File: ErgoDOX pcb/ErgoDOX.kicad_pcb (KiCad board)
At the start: 2 copper layers, 182.8 x 158.9 mm, 74 parts, among them J1 USB, J2 3.5mm, J3 JMP, J4 JMP, SW0:10 SW0:3, SW0:11 SW0:2, SW0:12 SW0:1, SW0:7 SW0:6, SW0:8 SW0:5, SW0:9 SW0:4, SW1:10 SW1:3, SW1:11 SW1:2, SW1:12 SW1:1, SW1:13 SW1:0, SW1:9 SW1:4, SW2:10 SW2:3, SW2:11 SW2:2, SW2:12 SW2:1, SW2:13 SW2:0, SW2:7 SW2:6, SW2:8 SW2:5, SW2:9 SW2:4, SW3:10 SW3:3, SW3:11 SW3:2, SW3:12 SW3:1, SW3:13 SW3:0, SW3:8 SW3:5, SW3:9 SW3:4, SW4:10 SW4:3, SW4:11 SW4:2, SW4:12 SW4:1, SW4:13 SW4:0, SW4:7 SW4:6, SW4:8 SW4:5, SW4:9 SW4:4, SW5:10 SW5:3, SW5:11 SW5:2, SW5:12 SW5:1, SW5:13 SW5:0, SW5:7 SW5:6, SW5:8 SW5:5, SW5:9 SW5:4, U1 TEENSY2.0, U2 MCP23018

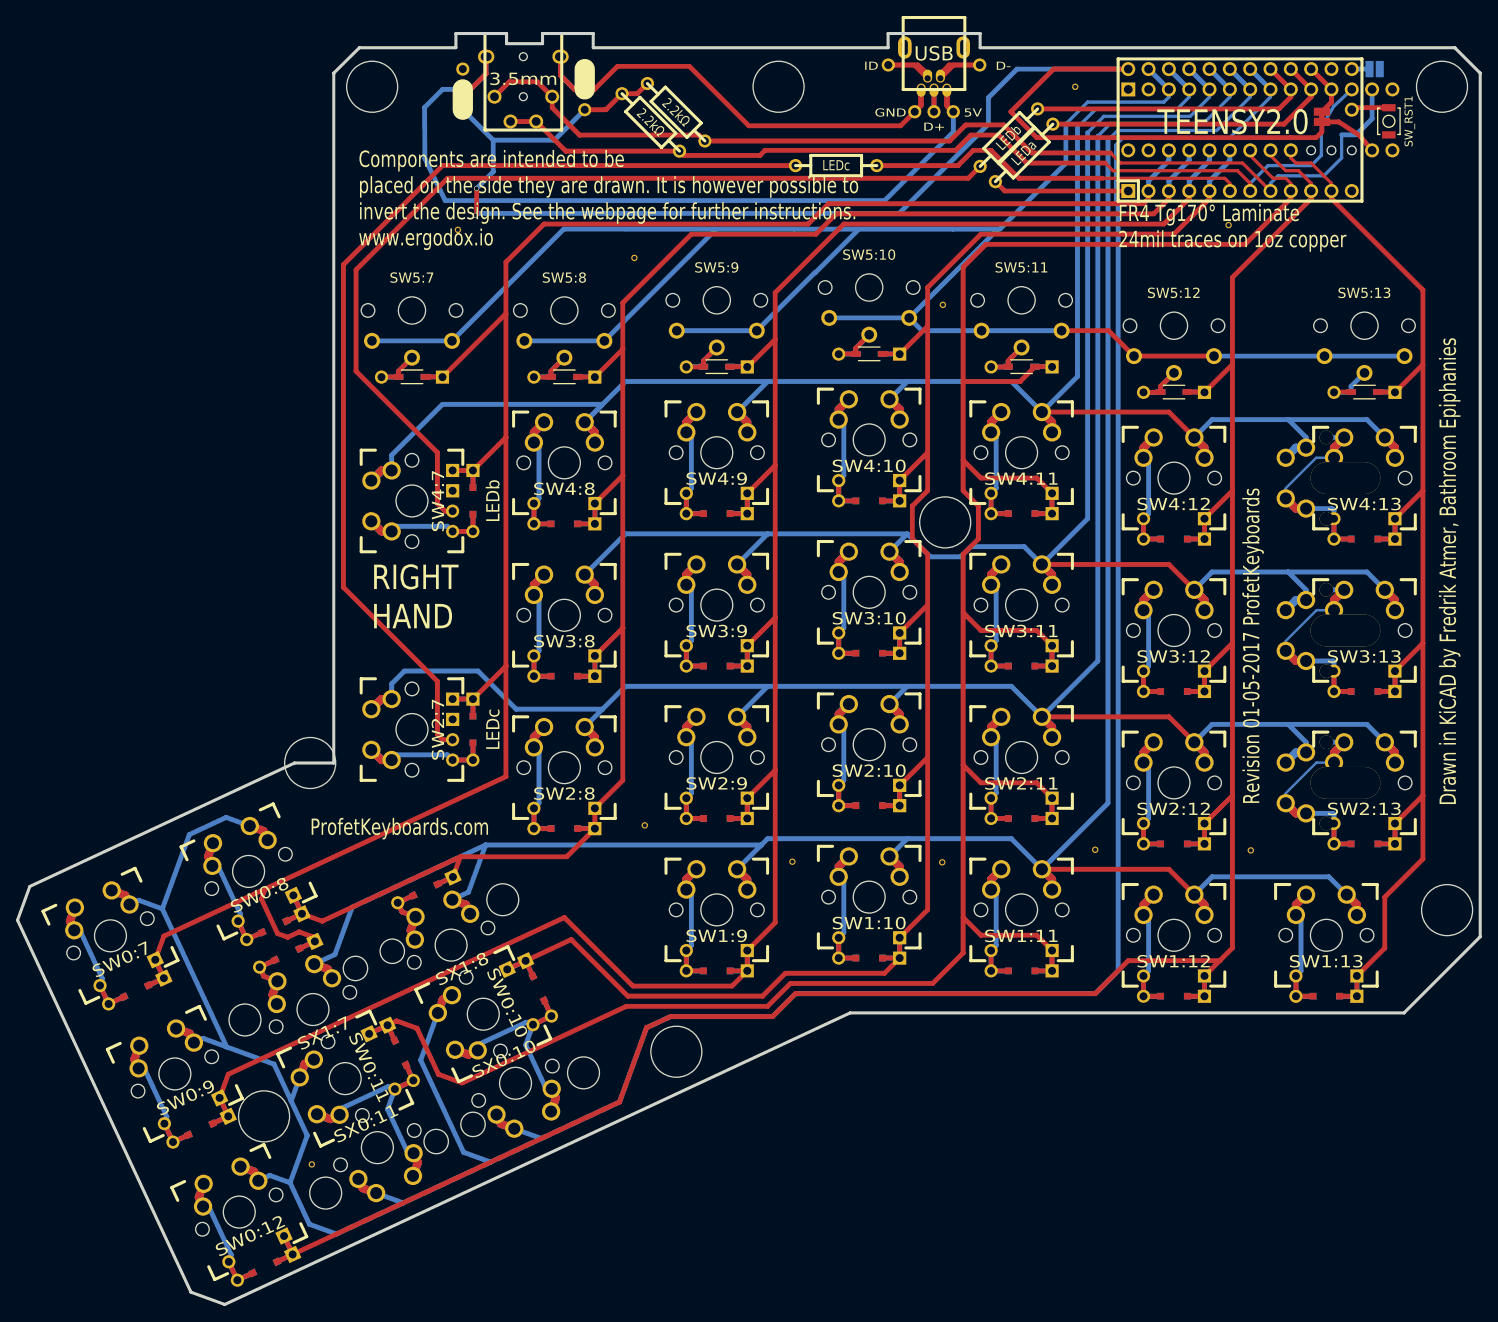
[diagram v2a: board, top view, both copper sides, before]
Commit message: finish replacing all switches
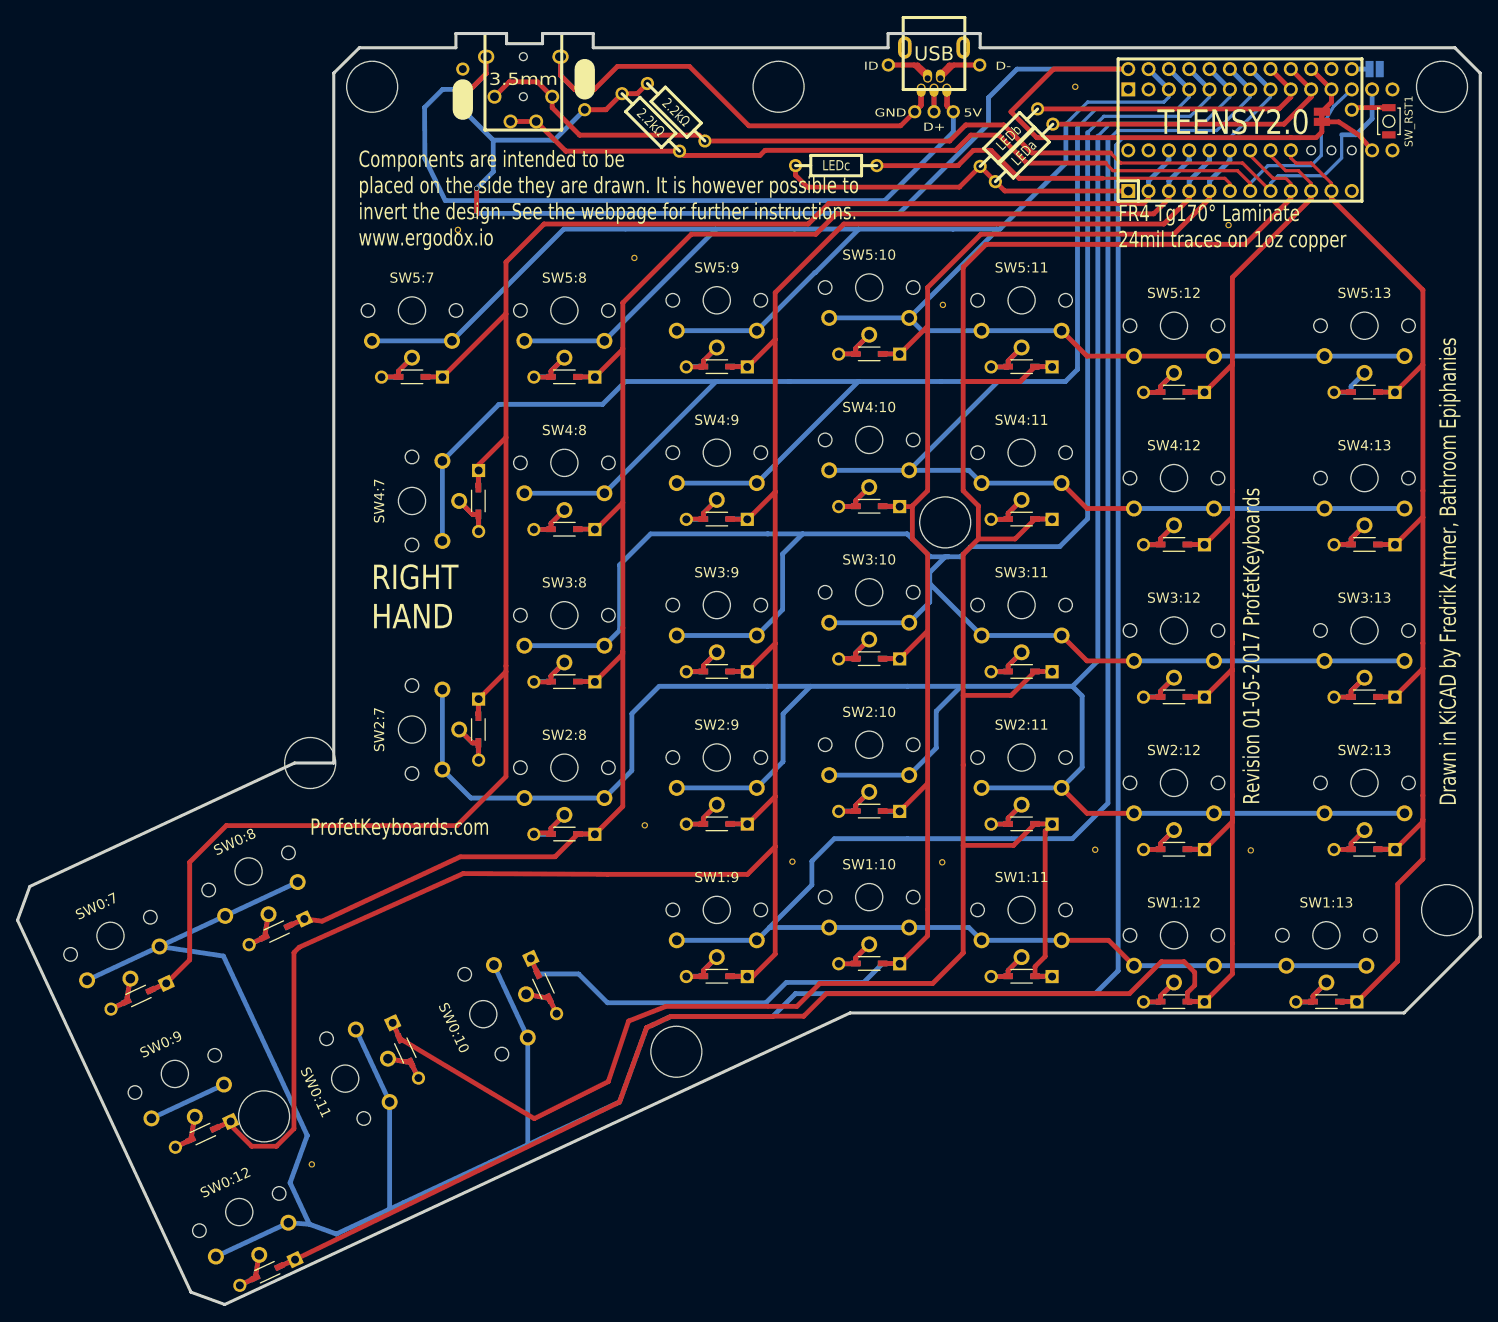
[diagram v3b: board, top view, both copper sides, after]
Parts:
- removed D1:7, D1:8: D, DIODE
- removed LED_B1: LEDb, MX_LED
- removed LED_C1: LEDc, MX_LED
- removed S1, S2: STAB200, STAB_PCB940
- removed SX0:10: SX0:3, MX_FLIP
- removed SX0:11: SX0:2, MX_FLIP
- removed SX1:7: SX1:6, MX_FLIP
- removed SX1:8: SX1:5, MX_FLIP
- SW0:10, SW0:11, SW0:12, SW0:7, SW0:8, SW0:9, SW1:10, SW1:11, SW1:12, SW1:13, SW1:9, SW2:10, SW2:11, SW2:12, SW2:7, SW2:8, SW2:9, SW3:10, SW3:11, SW3:12, SW3:8, SW3:9, SW4:10, SW4:11, SW4:12, SW4:7, SW4:8, SW4:9: footprint ErgoDOX pcb:MX_FLIP_DIODE -> ErgoDOX pcb:SW_choc_Reversible_1u
- SW2:13, SW3:13, SW4:13: footprint ErgoDOX pcb:MX_FLIP_XX -> ErgoDOX pcb:SW_choc_Reversible_1u
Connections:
- RB1 pad 2: Net-(LED_B1-Pad1) -> GND
- RC1 pad 2: Net-(LED_C1-Pad1) -> GND
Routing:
- net Net-(LED_C1-Pad1): track 127.4 -> 0.00 mm
- net Net-(LED_B1-Pad1): track 119.1 -> 0.00 mm
- net /ROW1: track 318.2 -> 246.8 mm
- net /ROW4: track 257.4 -> 292.0 mm
- net GND: track 19.3 -> 48.0 mm
- net Net-(SW3:13-Pad2): track 35.2 -> 10.4 mm
- net Net-(SW2:13-Pad2): track 35.2 -> 10.4 mm
- net Net-(SW4:13-Pad2): track 35.2 -> 10.4 mm
- net Net-(SW0:11-Pad2): track 34.8 -> 10.1 mm
- net Net-(SW0:10-Pad2): track 34.8 -> 10.1 mm
- net /ROW3: track 238.7 -> 263.0 mm
- net /COL4: track 273.4 -> 291.6 mm
- net /ROW0: track 404.2 -> 387.4 mm
- net /ROW2: track 295.3 -> 311.1 mm
- net Net-(D1:7-Pad1): track 12.3 -> 0.00 mm
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
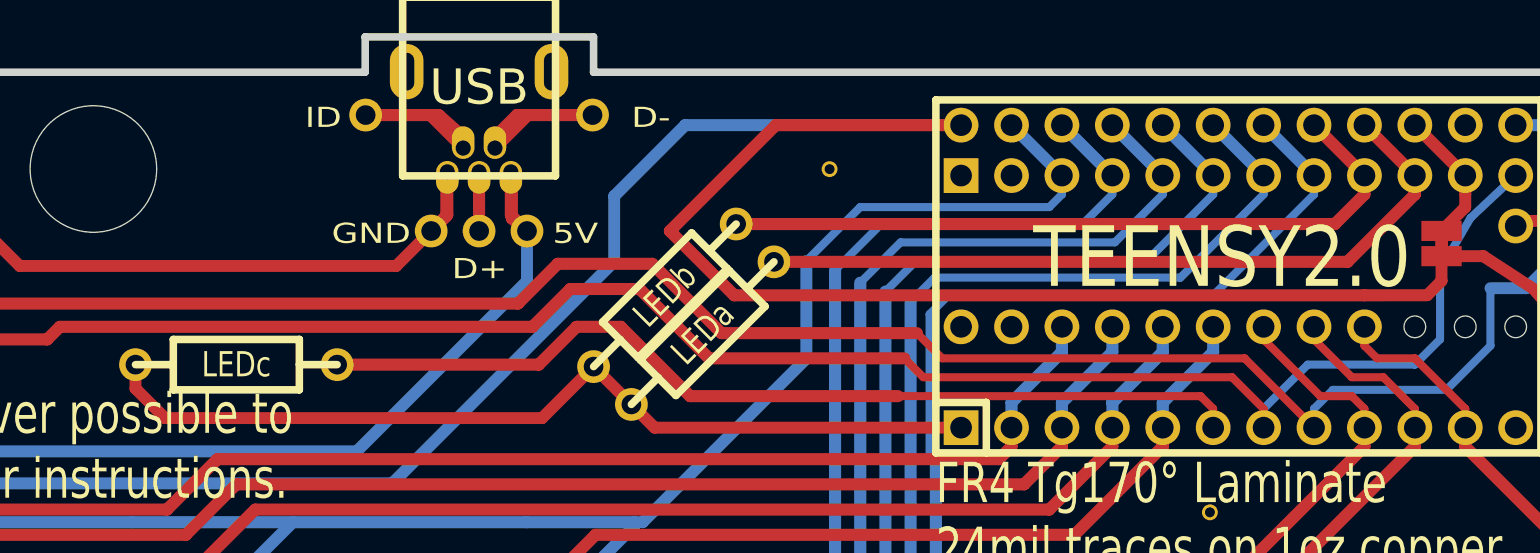
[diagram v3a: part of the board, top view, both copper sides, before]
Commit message: add usb c footprint file from https://github.com/ai03-2725/Type-C.pretty
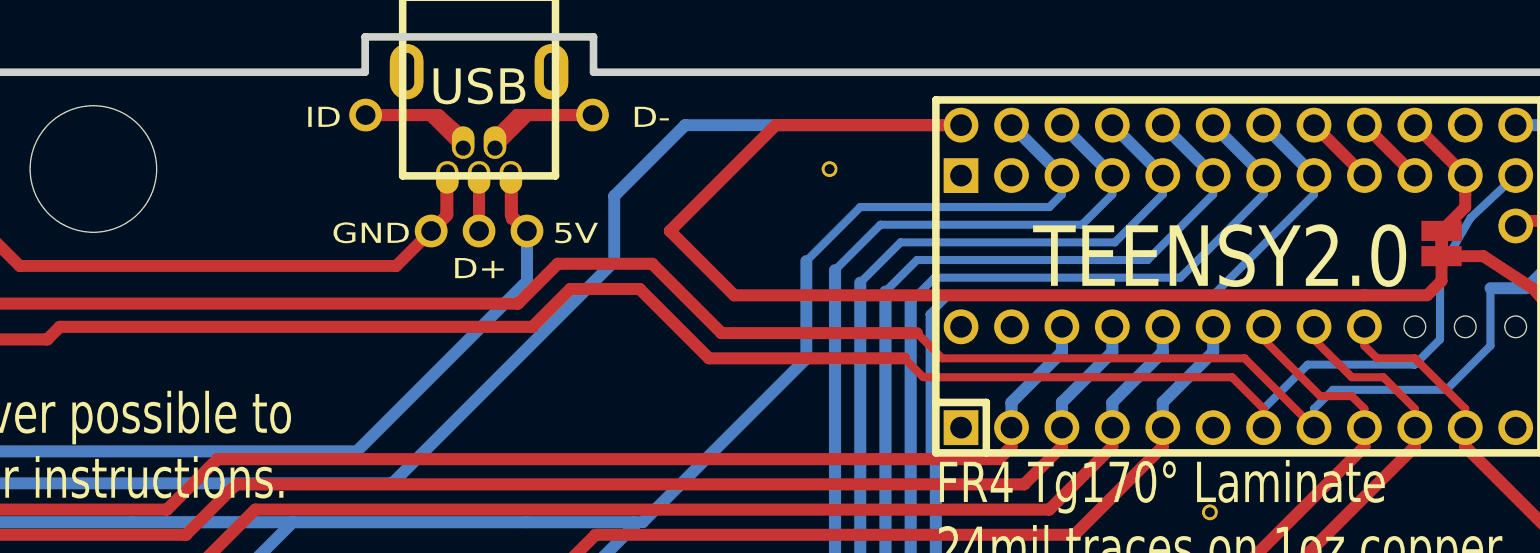
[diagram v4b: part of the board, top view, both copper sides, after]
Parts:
- removed RA1: LEDa, RESISTOR
- removed RB1: LEDb, RESISTOR
- removed RC1: LEDc, RESISTOR
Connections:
- U2 pad : Net-(U2-Pad19) -> (no net)
- U2 pad 14: Net-(U2-Pad14) -> unconnected-(U2-Pad14)
- U2 pad 28: Net-(U2-Pad28) -> unconnected-(U2-Pad28)
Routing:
- net /LED_C: track 47.6 -> 0.00 mm
- net GND: track 48.0 -> 2.22 mm
- net /LED_A: track 38.2 -> 3.59 mm
- net /LED_B: track 36.8 -> 3.59 mm
